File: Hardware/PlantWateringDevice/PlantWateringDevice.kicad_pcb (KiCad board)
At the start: 4 copper layers, 50 x 50 mm, 64 parts, among them J1 Conn_02x04_Counter_Clockwise, J2 USB_B, J5 Conn_02x03_Odd_Even, M1 Motor_DC, Q1 AO3404A, SW1 SW_DIP_x02, SW2 SW_Push, SW3 SW_Push, SW4 SW_DIP_x02, SW7 SW_DIP_x02, U1 MCP6002-xSN, U2 74LVC1G3157, U4 PIC10F202-IOT, U6 74HC74, U7 74HC4017D

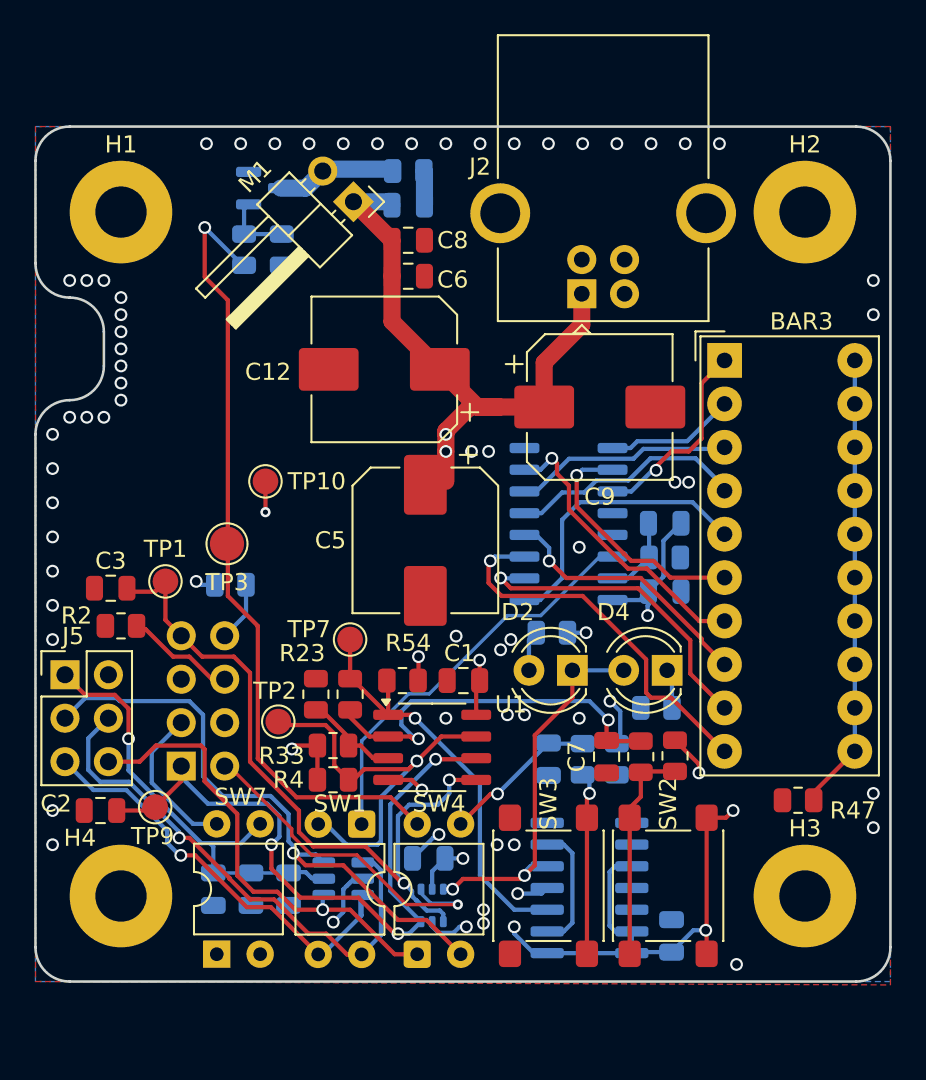
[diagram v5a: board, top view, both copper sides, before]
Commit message: fix #16, fix #17, fix #18, fix #19, fix #20, fix #26, fix #27, fix #28, fix #30, fix #32, fix#33, fix #34, fix #35, fix #38
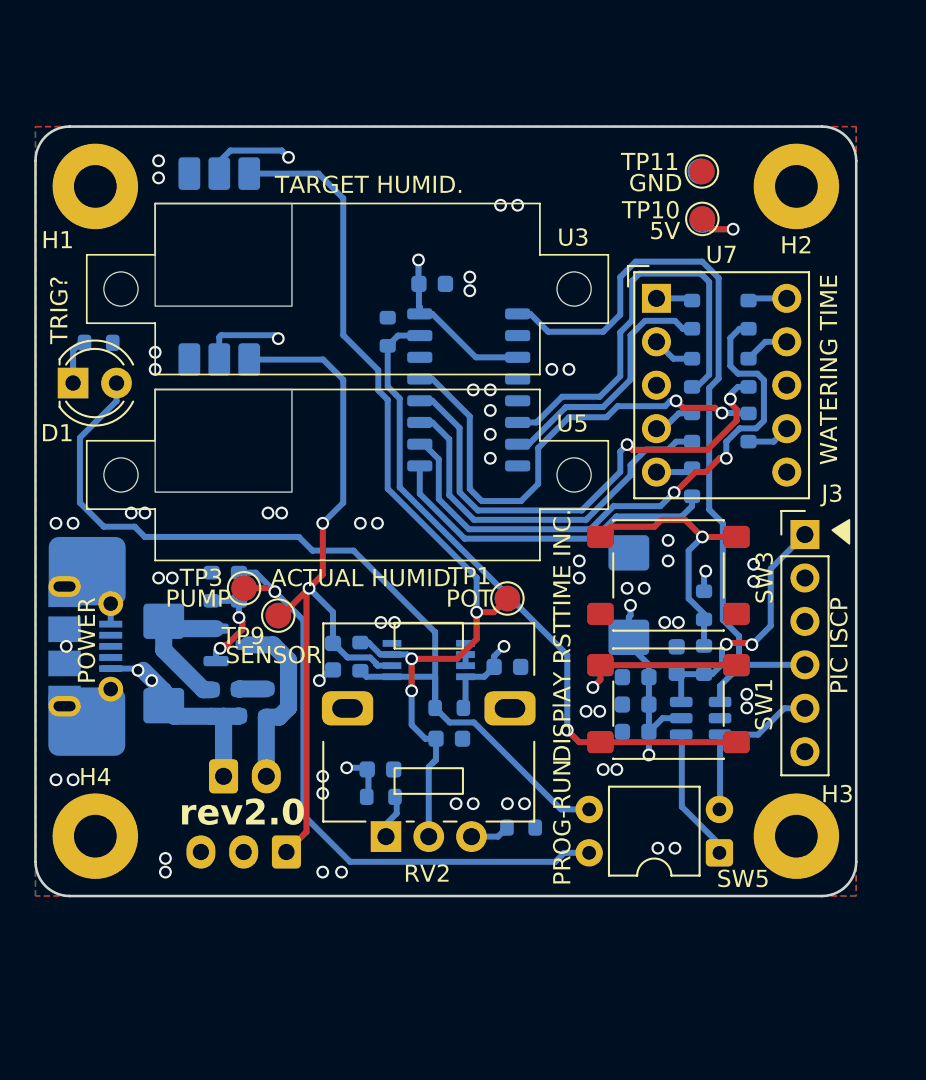
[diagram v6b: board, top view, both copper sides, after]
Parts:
- removed BAR3: HDSP-4830_2, Display:HDSP-4830
- removed C12: 470u/16v, Capacitor_SMD:CP_Elec_8x10
- removed C17, C21, C25: 100n, Capacitor_SMD:C_0805_2012Metric
- removed C8: 330n, Capacitor_SMD:C_0805_2012Metric
- removed D2, D4: LED, LED_THT:LED_D4.0mm
- removed J2: USB_B, Connector_USB:USB_B_OST_USB-B1HSxx_Horizontal
- removed J5: Conn_02x03_Odd_Even, Connector_PinHeader_2.54mm:PinHeader_2x03_P2.54mm_Vertical
- removed R11, R24, R33: 10k, Resistor_SMD:R_0805_2012Metric
- removed R31, R32: 510R, Resistor_SMD:R_0805_2012Metric
- removed R34: 100k, Resistor_SMD:R_0805_2012Metric
- removed R47: 120R, Resistor_SMD:R_0805_2012Metric
- removed R5: 47R, Resistor_SMD:R_0805_2012Metric
- removed R53: 22k, Resistor_SMD:R_0805_2012Metric
- removed R54: 1k, Resistor_SMD:R_0805_2012Metric
- removed SW2: SW_Push, Button_Switch_SMD:SW_SPST_PTS645Sx43SMTR92
- removed SW4, SW7: SW_DIP_x02, Package_DIP:DIP-4_W7.62mm
- removed TP2, TP7: TestPoint, TestPoint:TestPoint_Pad_D1.5mm
- removed U1: MCP6002-xSN, Package_SO:SO-8_3.9x4.9mm_P1.27mm
- added D1: LED, LED_THT:LED_D4.0mm, F.Cu at (137.2, 55.0)
- added J3: Conn_PIC_ICSP_ICD, Connector_PinHeader_2.54mm:PinHeader_1x06_P2.54mm_Vertical, F.Cu at (180.0, 63.9)
- added J4: Conn_01x03_Socket, Connector_JST:JST_EH_B3B-EH-A_1x03_P2.50mm_Vertical, B.Cu at (149.7, 82.4)
- added R10: TBD, Resistor_SMD:R_0603_1608Metric, B.Cu at (154.0, 71.0)
- added R12: 4R7, Resistor_SMD:R_0603_1608Metric, B.Cu at (148.5, 73.7)
- added R13: 120R, Resistor_SMD:R_0603_1608Metric, B.Cu at (176.7, 54.4)
- added R14: 10k, Resistor_SMD:R_0603_1608Metric, B.Cu at (155.6, 52.0)
- added R20: 120R, Resistor_SMD:R_0603_1608Metric, B.Cu at (176.7, 57.6)
- added R21: 120R, Resistor_SMD:R_0603_1608Metric, B.Cu at (173.4, 60.8)
- added R22: 120R, Resistor_SMD:R_0603_1608Metric, B.Cu at (173.4, 57.6)
- added R25: 120R, Resistor_SMD:R_0603_1608Metric, B.Cu at (173.4, 51.0)
- added R27: 120R, Resistor_SMD:R_0603_1608Metric, B.Cu at (176.7, 51.0)
- added R3: 510R, Resistor_SMD:R_0603_1608Metric, B.Cu at (138.7, 52.6)
- added RV2: R_Potentiometer, Potentiometer_THT:Potentiometer_Alps_RK09L_Single_Vertical, F.Cu at (155.5, 81.5)
- added SW5: SW_DIP_x02, Package_DIP:DIP-4_W7.62mm, F.Cu at (175.0, 82.5)
- added TP11: TestPoint, TestPoint:TestPoint_Pad_D1.5mm, F.Cu at (174.0, 42.6)
- added TP12: TestPoint, TestPoint:TestPoint_Pad_D1.5mm, B.Cu at (174.0, 45.5)
- added TP13: TestPoint, TestPoint:TestPoint_Pad_D1.5mm, B.Cu at (173.9, 42.6)
- added U3: ~, PlantWateringDevice:SegmentDisplayMounting, F.Cu at (153.2, 49.5)
- added U5: ~, PlantWateringDevice:SegmentDisplayMounting, F.Cu at (153.2, 60.4)
- C1, C2, C3, C6, C7: footprint Capacitor_SMD:C_0805_2012Metric -> Capacitor_SMD:C_0603_1608Metric; moved to B.Cu
- C13, C14, C15, C16, C18, C4: footprint Capacitor_SMD:C_0805_2012Metric -> Capacitor_SMD:C_0603_1608Metric
- C5, C9: value 470u/16v -> 100u/10v; footprint Capacitor_SMD:CP_Elec_8x10 -> Capacitor_Tantalum_SMD:CP_EIA-6032-28_Kemet-C; moved to B.Cu
- H1, H2, H3, H4: footprint MountingHole:MountingHole_3mm_Pad -> MountingHole:MountingHole_2.5mm_Pad
- J1: value Conn_02x04_Counter_Clockwise -> USB_B_Micro; footprint Connector_PinHeader_2.54mm:PinHeader_2x04_P2.54mm_Vertical -> PlantWateringDevice:USB_Micro-B_Molex-105017-0001_Extra_Mechanical_Pads
- M1: footprint Connector_PinHeader_2.54mm:PinHeader_1x02_P2.54mm_Horizontal -> Connector_JST:JST_EH_B2B-EH-A_1x02_P2.50mm_Vertical; moved to B.Cu
- R1, R6, R8: footprint Resistor_SMD:R_0805_2012Metric -> Resistor_SMD:R_0603_1608Metric
- R2, R4: footprint Resistor_SMD:R_0805_2012Metric -> Resistor_SMD:R_0603_1608Metric; moved to B.Cu
- R23: value 10k -> 120R; footprint Resistor_SMD:R_0805_2012Metric -> Resistor_SMD:R_0603_1608Metric; moved to B.Cu
- R7: value 10k -> 47R; footprint Resistor_SMD:R_0805_2012Metric -> Resistor_SMD:R_0603_1608Metric
- R9: value 4R7 -> 10k; footprint Resistor_SMD:R_0805_2012Metric -> Resistor_SMD:R_0603_1608Metric
- SW1: value SW_DIP_x02 -> SW_Push; footprint Package_DIP:DIP-4_W7.62mm -> Button_Switch_SMD:SW_SPST_PTS645Sx43SMTR92
- TP3: footprint TestPoint:TestPoint_Pad_D2.0mm -> TestPoint:TestPoint_Pad_D1.5mm
- U2: value 74LVC1G3157 -> LM2903; footprint Package_TO_SOT_SMD:SOT-363_SC-70-6 -> Package_SO:TSSOP-8_3x3mm_P0.65mm
- U6: value 74HC74 -> ~; footprint Package_SO:SO-14_3.9x8.65mm_P1.27mm -> Package_SO:JEITA_SOIC-16_3.9x9.9mm_P1.27mm
- U7: value 74HC4017D -> SC39-11EWA; footprint Package_SO:SO-16_3.9x9.9mm_P1.27mm -> Display_7Segment:Sx39-1xxxxx; moved to F.Cu
- moved M1 34.5 mm to (146.0, 78.0), turned to 0 degrees
- moved C4 33.6 mm to (158.2, 49.2), turned to 0 degrees
- moved C14 30.7 mm to (146.9, 73.7), turned to 90 degrees
- moved U6 30.0 mm to (160.3, 55.4), turned to 180 degrees
- moved TP10 29.8 mm to (174.0, 45.4)
- moved C9 29.6 mm to (142.5, 71.4), turned to 90 degrees
- moved R23 28.9 mm to (173.4, 54.4), turned to -90 degrees
- moved C6 27.5 mm to (145.3, 73.7), turned to 90 degrees
- moved C18 27.0 mm to (170.1, 73.8), turned to 180 degrees
- moved R9 26.9 mm to (145.3, 66.9), turned to -90 degrees
- moved Q1 26.8 mm to (146.5, 70.3)
- moved R2 26.2 mm to (163.4, 81.0), turned to 180 degrees
- moved C16 24.3 mm to (170.1, 75.4), turned to 180 degrees
- moved C15 23.8 mm to (170.1, 72.2), turned to 180 degrees
- moved U4 22.9 mm to (173.9, 74.6)
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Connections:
- C1 pad 1: VCC -> +5V
- C13 pad 1: BUTTON -> Net-(J3-~{MCLR}/VPP)
- C14 pad 1: VCC -> +5V
- C15 pad 1: Net-(J5-Pin_1) -> +5V
- C16 pad 1: Net-(J5-Pin_1) -> +5V
- C18 pad 1: Net-(J5-Pin_1) -> +5V
- C4 pad 1: VCC -> +5V
- C5 pad 1: VCC -> +5V
- C6 pad 1: VCC -> +5V
- C7 pad 1: Net-(U1A--) -> +5V
- C9 pad 1: VCC -> +5V
- J1 pad 1: HUMIDITY_SENSOR -> +5V
- J1 pad 2: LCD_DATA -> unconnected-(J1-D--Pad2)
- J1 pad 3: DISPLAY_POWER -> unconnected-(J1-D+-Pad3)
- J1 pad 4: VCC -> unconnected-(J1-ID-Pad4)
- M1 pad 1: VCC -> +5V
- R1 pad 1: POTENTIOMETER_VCC -> Net-(R1-Pad1)
- R1 pad 2: VCC -> +5V
- R2 pad 2: POTENTIOMETER_VSS -> Net-(R2-Pad2)
- R23 pad 1: Net-(U1A-+) -> Net-(U7-F)
- R23 pad 2: GND -> Net-(U6-F)
- R4 pad 2: VCC -> +5V
- R6 pad 1: VCC -> +5V
- R7 pad 2: GND -> PUMP_ON_OFF
- R8 pad 2: BUTTON -> Net-(J3-~{MCLR}/VPP)
- R9 pad 1: Net-(C14-Pad2) -> GND
- R9 pad 2: Net-(M1--) -> Net-(Q1-G)
- SW1 pad 1: DISPLAY_BARGRAPH -> Net-(U6-RES)
- SW1 pad 2: HUMIDITY_COMPARATION -> +5V
- TP10 pad 1: VCC -> +5V
- U2 pad 1: POTENTIOMETER_DATA -> HUMIDITY_COMPARATION
- U2 pad 2: GND -> HUMIDITY_SENSOR
- U2 pad 3: HUMIDITY_SENSOR -> POTENTIOMETER_DATA
- U2 pad 4: LCD_DATA -> GND
- U2 pad 5: VCC -> GND
- U2 pad 6: Net-(D2-K) -> Net-(U2B--)
- U4 pad 1: Net-(J5-Pin_4) -> BARGRAPH_DATA
- U4 pad 3: Net-(J5-Pin_5) -> Net-(J3-PGC/ICSPCLK)
- U4 pad 5: Net-(J5-Pin_1) -> +5V
- U4 pad 6: Net-(J5-Pin_3) -> Net-(J3-~{MCLR}/VPP)
- U6 pad 1: VCC -> BARGRAPH_DATA
- U6 pad 10: VCC -> Net-(U6-A)
- U6 pad 11: GND -> Net-(U6-E)
- U6 pad 12: GND -> Net-(U6-B)
- U6 pad 13: VCC -> Net-(U6-C)
- U6 pad 14: VCC -> unconnected-(U6-UCS-Pad14)
- U6 pad 2: Net-(U6A-D) -> GND
- U6 pad 3: Net-(U6A-C) -> +5V
- U6 pad 4: VCC -> unconnected-(U6-DEO-Pad4)
- U6 pad 5: Net-(D2-K) -> unconnected-(U6-CO-Pad5)
- U6 pad 6: Net-(U6A-D) -> Net-(U6-F)
- U6 pad 7: GND -> Net-(U6-G)
- U6 pad 8: unconnected-(U6B-~{Q}-Pad8) -> GND
- U6 pad 9: unconnected-(U6B-Q-Pad9) -> Net-(U6-D)
- U7 pad 2: Net-(U7-Q1) -> Net-(U7-F)
- U7 pad 3: Net-(U7-Q0) -> GND
- U7 pad 6: Net-(U7-Q7) -> unconnected-(U7-DP-Pad6)
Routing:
- net VCC: track 94.2 -> 0.00 mm, vias 15 -> 0
- net +5V: track 0.00 -> 66.2 mm, vias 0 -> 12
- net BARGRAPH_DATA: track 0.00 -> 45.7 mm
- net Net-(U6-RES): track 0.00 -> 39.1 mm, vias 0 -> 1
- net Net-(J5-Pin_3): track 35.2 -> 0.00 mm, vias 1 -> 0
- net Net-(U6-A): track 0.00 -> 34.1 mm, vias 0 -> 2
- net Net-(J5-Pin_4): track 30.9 -> 0.00 mm, vias 1 -> 0
- net HUMIDITY_COMPARATION: track 23.6 -> 54.0 mm, vias 1 -> 0
- net Net-(U6-B): track 0.00 -> 29.4 mm, vias 0 -> 2
- net Net-(U6-C): track 0.00 -> 28.6 mm, vias 0 -> 2
- net Net-(BAR3-K-Pad11): track 26.3 -> 0.00 mm
- net Net-(J5-Pin_1): track 25.8 -> 0.00 mm, vias 1 -> 0
- net Net-(J5-Pin_5): track 25.2 -> 0.00 mm, vias 1 -> 0
- net Net-(U6-F): track 0.00 -> 24.1 mm
- net Net-(U6A-C): track 23.8 -> 0.00 mm, vias 1 -> 0
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- added copper zone on In2.Cu, net +5V
- added copper zone on In1.Cu, net GND
- removed copper zone on In2.Cu, net GND
- removed copper zone on In1.Cu, net VCC
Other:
- board size 50 x 50 mm -> 48 x 45 mm
- board text added: "5V"
- board text added: "ACTUAL HUMID."
- board text added: "DISPlAY RST"
- board text added: "GND"
- board text added: "PIC ISCP"
- board text added: "POT"
- board text added: "POWER"
- board text added: "PROG-RUN"
- board text added: "PUMP"
- board text added: "SENSOR"
- board text added: "TARGET HUMID."
- board text added: "TIME INC."
- board text added: "TRIG?"
- board text added: "WATERING TIME"
- board text added: "rev2.0"
